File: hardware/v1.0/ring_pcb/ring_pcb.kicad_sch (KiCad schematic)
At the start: 7 parts

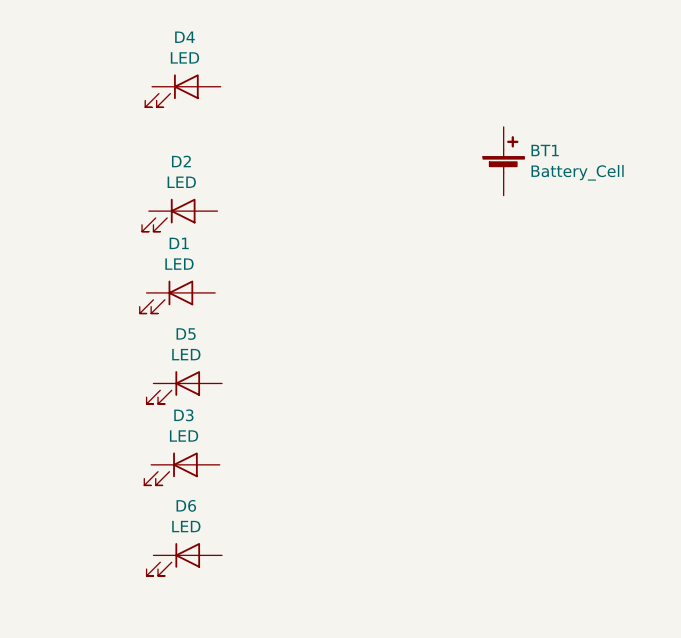
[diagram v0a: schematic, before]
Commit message: Add test pads
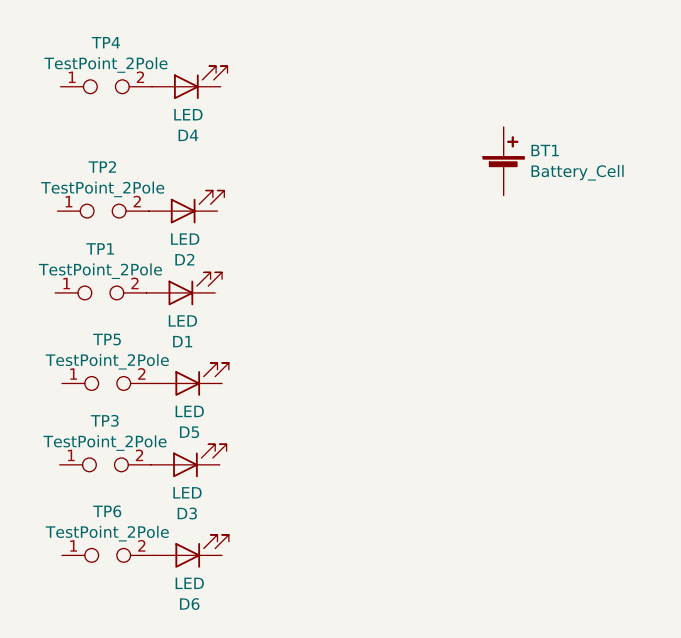
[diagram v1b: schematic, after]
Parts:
- added TP1, TP2, TP3, TP4, TP5, TP6: TestPoint_2Pole, TestPoint:TestPoint_2Pads_Pitch2.54mm_Drill0.8mm, symbol Connector:TestPoint_2Pole
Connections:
- net at D4.2 (A): now also TP4.2
- net at D5.2 (A): now also TP5.2
- net at D3.2 (A): now also TP3.2
- net at D2.2 (A): now also TP2.2
- net at D6.2 (A): now also TP6.2
- net at D1.2 (A): now also TP1.2
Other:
- moved on the sheet: D1, D2, D3, D4, D5, D6
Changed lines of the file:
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@@
 (kicad_sch (version 20201015) (generator eeschema)
   (paper "A4")
-  (symbol (lib_id "Device:LED") (at 121.8184 87.7824 0) (unit 1)
+  (symbol (lib_id "Connector:TestPoint_2Pole") (at 112.9284 87.7824 0) (unit 1)
     (in_bom yes) (on_board yes)
-    (property "Reference" "D1" (id 0) (at 121.6279 82.3276 0))
-    (property "Value" "LED" (id 1) (at 121.6279 84.6263 0))
+    (property "Reference" "TP1" (id 0) (at 112.9284 82.9372 0))
+    (property "Value" "TestPoint_2Pole" (id 1) (at 112.9284 85.2359 0))
+    (property "Footprint" "TestPoint:TestPoint_2Pads_Pitch2.54mm_Drill0.8mm" (id 2) (at 112.9284 87.7824 0)
+      (effects (font (size 1.27 1.27)) hide)
+    )
+    (property "Datasheet" "~" (id 3) (at 112.9284 87.7824 0)
+      (effects (font (size 1.27 1.27)) hide)
+    )
+  )
+  (symbol (lib_id "Connector:TestPoint_2Pole") (at 113.1824 78.6892 0) (unit 1)
+    (in_bom yes) (on_board yes)
+    (property "Reference" "TP2" (id 0) (at 113.1824 73.844 0))
+    (property "Value" "TestPoint_2Pole" (id 1) (at 113.1824 76.1427 0))
+    (property "Footprint" "TestPoint:TestPoint_2Pads_Pitch2.54mm_Drill0.8mm" (id 2) (at 113.1824 78.6892 0)
+      (effects (font (size 1.27 1.27)) hide)
+    )
+    (property "Datasheet" "~" (id 3) (at 113.1824 78.6892 0)
+      (effects (font (size 1.27 1.27)) hide)
+    )
+  )
+  (symbol (lib_id "Connector:TestPoint_2Pole") (at 113.4364 106.8832 0) (unit 1)
+    (in_bom yes) (on_board yes)
+    (property "Reference" "TP3" (id 0) (at 113.4364 102.038 0))
+    (property "Value" "TestPoint_2Pole" (id 1) (at 113.4364 104.3367 0))
+    (property "Footprint" "TestPoint:TestPoint_2Pads_Pitch2.54mm_Drill0.8mm" (id 2) (at 113.4364 106.8832 0)
+      (effects (font (size 1.27 1.27)) hide)
+    )
+    (property "Datasheet" "~" (id 3) (at 113.4364 106.8832 0)
+      (effects (font (size 1.27 1.27)) hide)
+    )
+  )
+  (symbol (lib_id "Connector:TestPoint_2Pole") (at 113.538 64.8716 0) (unit 1)
+    (in_bom yes) (on_board yes)
+    (property "Reference" "TP4" (id 0) (at 113.538 60.0264 0))
+    (property "Value" "TestPoint_2Pole" (id 1) (at 113.538 62.3251 0))
+    (property "Footprint" "TestPoint:TestPoint_2Pads_Pitch2.54mm_Drill0.8mm" (id 2) (at 113.538 64.8716 0)
+      (effects (font (size 1.27 1.27)) hide)
+    )
+    (property "Datasheet" "~" (id 3) (at 113.538 64.8716 0)
+      (effects (font (size 1.27 1.27)) hide)
+    )
+  )
+  (symbol (lib_id "Connector:TestPoint_2Pole") (at 113.6904 97.8408 0) (unit 1)
+    (in_bom yes) (on_board yes)
+    (property "Reference" "TP5" (id 0) (at 113.6904 92.9956 0))
+    (property "Value" "TestPoint_2Pole" (id 1) (at 113.6904 95.2943 0))
+    (property "Footprint" "TestPoint:TestPoint_2Pads_Pitch2.54mm_Drill0.8mm" (id 2) (at 113.6904 97.8408 0)
+      (effects (font (size 1.27 1.27)) hide)
+    )
+    (property "Datasheet" "~" (id 3) (at 113.6904 97.8408 0)
+      (effects (font (size 1.27 1.27)) hide)
+    )
+  )
+  (symbol (lib_id "Connector:TestPoint_2Pole") (at 113.6904 116.9416 0) (unit 1)
+    (in_bom yes) (on_board yes)
+    (property "Reference" "TP6" (id 0) (at 113.6904 112.0964 0))
+    (property "Value" "TestPoint_2Pole" (id 1) (at 113.6904 114.3951 0))
+    (property "Footprint" "TestPoint:TestPoint_2Pads_Pitch2.54mm_Drill0.8mm" (id 2) (at 113.6904 116.9416 0)
+      (effects (font (size 1.27 1.27)) hide)
+    )
+    (property "Datasheet" "~" (id 3) (at 113.6904 116.9416 0)
+      (effects (font (size 1.27 1.27)) hide)
+    )
+  )
+  (symbol (lib_id "Device:LED") (at 121.8184 87.7824 180) (unit 1)
+    (in_bom yes) (on_board yes)
+    (property "Reference" "D1" (id 0) (at 122.0089 93.2372 0))
+    (property "Value" "LED" (id 1) (at 122.0089 90.9385 0))
     (property "Footprint" "LED_SMD:LED_1206_3216Metric" (id 2) (at 121.8184 87.7824 0)
       (effects (font (size 1.27 1.27)) hide)
@@
     )
   )
-  (symbol (lib_id "Device:LED") (at 122.0724 78.6892 0) (unit 1)
+  (symbol (lib_id "Device:LED") (at 122.0724 78.6892 180) (unit 1)
     (in_bom yes) (on_board yes)
-    (property "Reference" "D2" (id 0) (at 121.8819 73.2344 0))
-    (property "Value" "LED" (id 1) (at 121.8819 75.5331 0))
+    (property "Reference" "D2" (id 0) (at 122.2629 84.144 0))
+    (property "Value" "LED" (id 1) (at 122.2629 81.8453 0))
     (property "Footprint" "LED_SMD:LED_1206_3216Metric" (id 2) (at 122.0724 78.6892 0)
       (effects (font (size 1.27 1.27)) hide)
@@
     )
   )
-  (symbol (lib_id "Device:LED") (at 122.3264 106.8832 0) (unit 1)
+  (symbol (lib_id "Device:LED") (at 122.3264 106.8832 180) (unit 1)
     (in_bom yes) (on_board yes)
-    (property "Reference" "D3" (id 0) (at 122.1359 101.4284 0))
-    (property "Value" "LED" (id 1) (at 122.1359 103.7271 0))
+    (property "Reference" "D3" (id 0) (at 122.5169 112.338 0))
+    (property "Value" "LED" (id 1) (at 122.5169 110.0393 0))
     (property "Footprint" "LED_SMD:LED_1206_3216Metric" (id 2) (at 122.3264 106.8832 0)
       (effects (font (size 1.27 1.27)) hide)
@@
     )
   )
-  (symbol (lib_id "Device:LED") (at 122.428 64.8716 0) (unit 1)
+  (symbol (lib_id "Device:LED") (at 122.428 64.8716 180) (unit 1)
     (in_bom yes) (on_board yes)
-    (property "Reference" "D4" (id 0) (at 122.2375 59.4168 0))
-    (property "Value" "LED" (id 1) (at 122.2375 61.7155 0))
+    (property "Reference" "D4" (id 0) (at 122.6185 70.3264 0))
+    (property "Value" "LED" (id 1) (at 122.6185 68.0277 0))
     (property "Footprint" "LED_SMD:LED_1206_3216Metric" (id 2) (at 122.428 64.8716 0)
       (effects (font (size 1.27 1.27)) hide)
@@
     )
   )
-  (symbol (lib_id "Device:LED") (at 122.5804 97.8408 0) (unit 1)
+  (symbol (lib_id "Device:LED") (at 122.5804 97.8408 180) (unit 1)
     (in_bom yes) (on_board yes)
-    (property "Reference" "D5" (id 0) (at 122.3899 92.386 0))
-    (property "Value" "LED" (id 1) (at 122.3899 94.6847 0))
+    (property "Reference" "D5" (id 0) (at 122.7709 103.2956 0))
+    (property "Value" "LED" (id 1) (at 122.7709 100.9969 0))
     (property "Footprint" "LED_SMD:LED_1206_3216Metric" (id 2) (at 122.5804 97.8408 0)
       (effects (font (size 1.27 1.27)) hide)
@@
     )
   )
-  (symbol (lib_id "Device:LED") (at 122.5804 116.9416 0) (unit 1)
+  (symbol (lib_id "Device:LED") (at 122.5804 116.9416 180) (unit 1)
     (in_bom yes) (on_board yes)
-    (property "Reference" "D6" (id 0) (at 122.3899 111.4868 0))
-    (property "Value" "LED" (id 1) (at 122.3899 113.7855 0))
+    (property "Reference" "D6" (id 0) (at 122.7709 122.3964 0))
+    (property "Value" "LED" (id 1) (at 122.7709 120.0977 0))
     (property "Footprint" "LED_SMD:LED_1206_3216Metric" (id 2) (at 122.5804 116.9416 0)
       (effects (font (size 1.27 1.27)) hide)
@@
       (reference "D6") (unit 1) (value "LED") (footprint "LED_SMD:LED_1206_3216Metric")
     )
+    (path "/dac0ea82-4c0b-4f2c-ab77-dc600c7a96ad"
+      (reference "TP1") (unit 1) (value "TestPoint_2Pole") (footprint "TestPoint:TestPoint_2Pads_Pitch2.54mm_Drill0.8mm")
+    )
+    (path "/a9daf2b0-0d7c-4b93-aec8-eed29e73de24"
+      (reference "TP2") (unit 1) (value "TestPoint_2Pole") (footprint "TestPoint:TestPoint_2Pads_Pitch2.54mm_Drill0.8mm")
+    )
+    (path "/3b640c0d-69f3-4f3f-aa12-a733dd6c425e"
+      (reference "TP3") (unit 1) (value "TestPoint_2Pole") (footprint "TestPoint:TestPoint_2Pads_Pitch2.54mm_Drill0.8mm")
+    )
+    (path "/5e7ebfcb-fcc9-4094-bdd0-2c1d9e20b15a"
+      (reference "TP4") (unit 1) (value "TestPoint_2Pole") (footprint "TestPoint:TestPoint_2Pads_Pitch2.54mm_Drill0.8mm")
+    )
+    (path "/a4e0b169-35a4-430b-9ac0-52d72ac5d2cf"
+      (reference "TP5") (unit 1) (value "TestPoint_2Pole") (footprint "TestPoint:TestPoint_2Pads_Pitch2.54mm_Drill0.8mm")
+    )
+    (path "/b252d9d5-175b-45d3-8347-b5f53ded0837"
+      (reference "TP6") (unit 1) (value "TestPoint_2Pole") (footprint "TestPoint:TestPoint_2Pads_Pitch2.54mm_Drill0.8mm")
+    )
   )

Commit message: First v0.1 cut
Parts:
- removed BT1: Battery_Cell, Battery:BatteryHolder_LINX_BAT-HLD-012-SMT, symbol Device:Battery_Cell
- added TP7, TP8: TestPoint_2Pole, Connector_Wire:SolderWirePad_1x02_P3.81mm_Drill1.2mm, symbol Connector:TestPoint_2Pole
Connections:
- net GND: now reaches D4.1 (K)
- net GND: now also D1.1 (K), D2.1 (K), D3.1 (K), D5.1 (K), D6.1 (K), TP7.1, TP8.1
- no-connect marks 0 -> 8
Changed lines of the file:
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@@
 (kicad_sch (version 20201015) (generator eeschema)
   (paper "A4")
+  (junction (at 125.6284 87.7824) (diameter 1.016) (color 0 0 0 0))
+  (junction (at 125.8824 78.6892) (diameter 1.016) (color 0 0 0 0))
+  (junction (at 126.1364 106.8832) (diameter 1.016) (color 0 0 0 0))
+  (junction (at 126.3904 97.8408) (diameter 1.016) (color 0 0 0 0))
+  (junction (at 126.3904 116.9416) (diameter 1.016) (color 0 0 0 0))
+  (no_connect (at 108.458 64.8716))
+  (no_connect (at 107.8484 87.7824))
+  (no_connect (at 108.1024 78.6892))
+  (no_connect (at 108.3564 106.8832))
+  (no_connect (at 108.6104 97.8408))
+  (no_connect (at 108.6104 116.9416))
+  (no_connect (at 138.0236 116.9416))
+  (no_connect (at 136.5504 97.8408))
+  (wire (pts (xy 125.6284 87.7824) (xy 125.6284 92.5576))
+    (stroke (width 0) (type solid) (color 0 0 0 0))
+  )
+  (wire (pts (xy 125.6284 87.7824) (xy 125.8824 87.7824))
+    (stroke (width 0) (type solid) (color 0 0 0 0))
+  )
+  (wire (pts (xy 125.6284 92.5576) (xy 126.3904 92.5576))
+    (stroke (width 0) (type solid) (color 0 0 0 0))
+  )
+  (wire (pts (xy 125.8824 74.2188) (xy 125.8824 78.6892))
+    (stroke (width 0) (type solid) (color 0 0 0 0))
+  )
+  (wire (pts (xy 125.8824 78.6892) (xy 125.8824 87.7824))
+    (stroke (width 0) (type solid) (color 0 0 0 0))
+  )
+  (wire (pts (xy 126.1364 99.9236) (xy 126.3904 99.9236))
+    (stroke (width 0) (type solid) (color 0 0 0 0))
+  )
+  (wire (pts (xy 126.1364 106.8832) (xy 126.1364 99.9236))
+    (stroke (width 0) (type solid) (color 0 0 0 0))
+  )
+  (wire (pts (xy 126.1364 108.7628) (xy 126.1364 106.8832))
+    (stroke (width 0) (type solid) (color 0 0 0 0))
+  )
+  (wire (pts (xy 126.238 64.8716) (xy 126.238 74.2188))
+    (stroke (width 0) (type solid) (color 0 0 0 0))
+  )
+  (wire (pts (xy 126.238 74.2188) (xy 125.8824 74.2188))
+    (stroke (width 0) (type solid) (color 0 0 0 0))
+  )
+  (wire (pts (xy 126.3904 92.5576) (xy 126.3904 97.8408))
+    (stroke (width 0) (type solid) (color 0 0 0 0))
+  )
+  (wire (pts (xy 126.3904 99.9236) (xy 126.3904 97.8408))
+    (stroke (width 0) (type solid) (color 0 0 0 0))
+  )
+  (wire (pts (xy 126.3904 108.7628) (xy 126.1364 108.7628))
+    (stroke (width 0) (type solid) (color 0 0 0 0))
+  )
+  (wire (pts (xy 126.3904 108.7628) (xy 126.3904 116.9416))
+    (stroke (width 0) (type solid) (color 0 0 0 0))
+  )
+  (wire (pts (xy 126.3904 116.9416) (xy 126.3904 117.7036))
+    (stroke (width 0) (type solid) (color 0 0 0 0))
+  )
+  (wire (pts (xy 126.3904 116.9416) (xy 127.8636 116.9416))
+    (stroke (width 0) (type solid) (color 0 0 0 0))
+  )
+  (wire (pts (xy 126.3904 117.7036) (xy 126.4412 117.7036))
+    (stroke (width 0) (type solid) (color 0 0 0 0))
+  )
+  (wire (pts (xy 126.4412 117.7036) (xy 126.4412 118.4656))
+    (stroke (width 0) (type solid) (color 0 0 0 0))
+  )
+  (symbol (lib_id "power:GND") (at 126.4412 118.4656 0) (unit 1)
+    (in_bom yes) (on_board yes)
+    (property "Reference" "#PWR0101" (id 0) (at 126.4412 124.8156 0)
+      (effects (font (size 1.27 1.27)) hide)
+    )
+    (property "Value" "GND" (id 1) (at 126.5555 122.79 0))
+    (property "Footprint" "" (id 2) (at 126.4412 118.4656 0)
+      (effects (font (size 1.27 1.27)) hide)
+    )
+    (property "Datasheet" "" (id 3) (at 126.4412 118.4656 0)
+      (effects (font (size 1.27 1.27)) hide)
+    )
+  )
   (symbol (lib_id "Connector:TestPoint_2Pole") (at 112.9284 87.7824 0) (unit 1)
     (in_bom yes) (on_board yes)
@@
     )
   )
+  (symbol (lib_id "Connector:TestPoint_2Pole") (at 131.4704 97.8408 0) (unit 1)
+    (in_bom yes) (on_board yes)
+    (property "Reference" "TP8" (id 0) (at 131.4704 92.9956 0))
+    (property "Value" "TestPoint_2Pole" (id 1) (at 131.4704 95.2943 0))
+    (property "Footprint" "Connector_Wire:SolderWirePad_1x02_P3.81mm_Drill1.2mm" (id 2) (at 131.4704 97.8408 0)
+      (effects (font (size 1.27 1.27)) hide)
+    )
+    (property "Datasheet" "~" (id 3) (at 131.4704 97.8408 0)
+      (effects (font (size 1.27 1.27)) hide)
+    )
+  )
+  (symbol (lib_id "Connector:TestPoint_2Pole") (at 132.9436 116.9416 0) (unit 1)
+    (in_bom yes) (on_board yes)
+    (property "Reference" "TP7" (id 0) (at 132.9436 112.0964 0))
+    (property "Value" "TestPoint_2Pole" (id 1) (at 132.9436 114.3951 0))
+    (property "Footprint" "Connector_Wire:SolderWirePad_1x02_P3.81mm_Drill1.2mm" (id 2) (at 132.9436 116.9416 0)
+      (effects (font (size 1.27 1.27)) hide)
+    )
+    (property "Datasheet" "~" (id 3) (at 132.9436 116.9416 0)
+      (effects (font (size 1.27 1.27)) hide)
+    )
+  )
   (symbol (lib_id "Device:LED") (at 121.8184 87.7824 180) (unit 1)
     (in_bom yes) (on_board yes)
@@
     )
   )
-  (symbol (lib_id "Device:Battery_Cell") (at 157.6832 74.422 0) (unit 1)
-    (in_bom yes) (on_board yes)
-    (property "Reference" "BT1" (id 0) (at 160.6043 72.0026 0)
-      (effects (font (size 1.27 1.27)) (justify left))
-    )
-    (property "Value" "Battery_Cell" (id 1) (at 160.6043 74.3013 0)
-      (effects (font (size 1.27 1.27)) (justify left))
-    )
-    (property "Footprint" "Battery:BatteryHolder_LINX_BAT-HLD-012-SMT" (id 2) (at 157.6832 72.898 90)
-      (effects (font (size 1.27 1.27)) hide)
-    )
-    (property "Datasheet" "~" (id 3) (at 157.6832 72.898 90)
-      (effects (font (size 1.27 1.27)) hide)
-    )
-  )
   (sheet_instances
     (path "/" (page "1"))
   )
   (symbol_instances
-    (path "/7f23df0d-c5f1-4fc3-b7fe-c7e90ce83fc7"
-      (reference "BT1") (unit 1) (value "Battery_Cell") (footprint "Battery:BatteryHolder_LINX_BAT-HLD-012-SMT")
+    (path "/3a654da8-ff45-4a1d-a535-cda78a2ba341"
+      (reference "#PWR0101") (unit 1) (value "GND") (footprint "")
     )
     (path "/f86d50c5-128d-459b-974c-e0abf9f5794b"
@@
       (reference "TP6") (unit 1) (value "TestPoint_2Pole") (footprint "TestPoint:TestPoint_2Pads_Pitch2.54mm_Drill0.8mm")
     )
-  )
+    (path "/5d1d4b9e-26cd-49ce-9a48-1f08d40d65d5"
+      (reference "TP7") (unit 1) (value "TestPoint_2Pole") (footprint "Connector_Wire:SolderWirePad_1x02_P3.81mm_Drill1.2mm")
+    )
+    (path "/695df2d6-462a-4d24-81ce-81457d22234a"
+      (reference "TP8") (unit 1) (value "TestPoint_2Pole") (footprint "Connector_Wire:SolderWirePad_1x02_P3.81mm_Drill1.2mm")
+    )
+  )

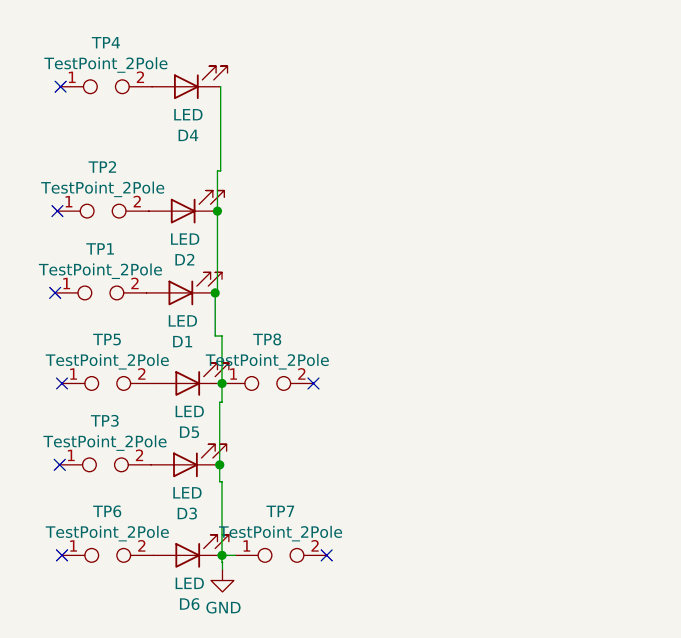
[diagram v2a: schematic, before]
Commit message: Update pcb to v0.2 for new mounting plan
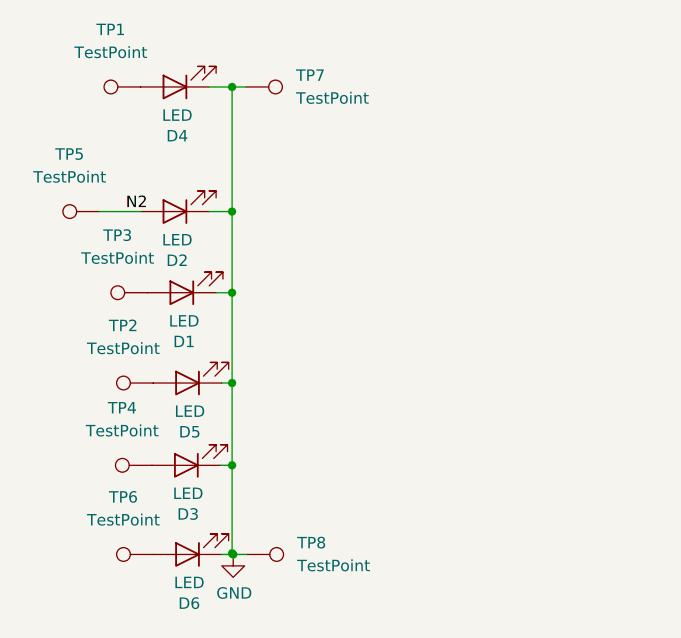
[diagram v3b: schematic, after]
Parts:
- removed TP1, TP2, TP3, TP4, TP5, TP6: TestPoint_2Pole, TestPoint:TestPoint_2Pads_Pitch2.54mm_Drill0.8mm, symbol Connector:TestPoint_2Pole
- removed TP7, TP8: TestPoint_2Pole, Connector_Wire:SolderWirePad_1x02_P3.81mm_Drill1.2mm, symbol Connector:TestPoint_2Pole
- added TP1, TP2, TP3, TP4, TP5, TP6, TP7, TP8: TestPoint, TestPoint:TestPoint_Pad_1.5x1.5mm, symbol Connector:TestPoint
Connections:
- net GND: now also TP8.1; no longer D1.1 (K), D2.1 (K), D3.1 (K), D4.1 (K), D5.1 (K)
- net at D4.2 (A): now also TP1.1
- net at D5.2 (A): now also TP2.1
- net at D3.2 (A): now also TP4.1
- net N2: now reaches D2.2 (A)
- net N2: now also TP5.1
- net at D6.2 (A): now also TP6.1
- net at D1.2 (A): now also TP3.1
- new net: D1.1 (K), D2.1 (K), D3.1 (K), D4.1 (K), D5.1 (K), TP7.1
- no-connect marks 8 -> 0
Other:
- moved on the sheet: D2, D4
